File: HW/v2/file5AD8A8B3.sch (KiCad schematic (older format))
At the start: 45 parts, among them J14 Barrel_Jack, U17 LT1054 neg5v, U18 INA219, U19 LM7805, U20 LM1117-3.3, U21 Vref, U22 AD8628, U23 LM321

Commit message: friday layout
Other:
- note added: "Neg supply"
- note added: "vREF"
- moved on the sheet: C33, C34, C36, C37, C38, C40, C42, D5, D6, D7, D8, D9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

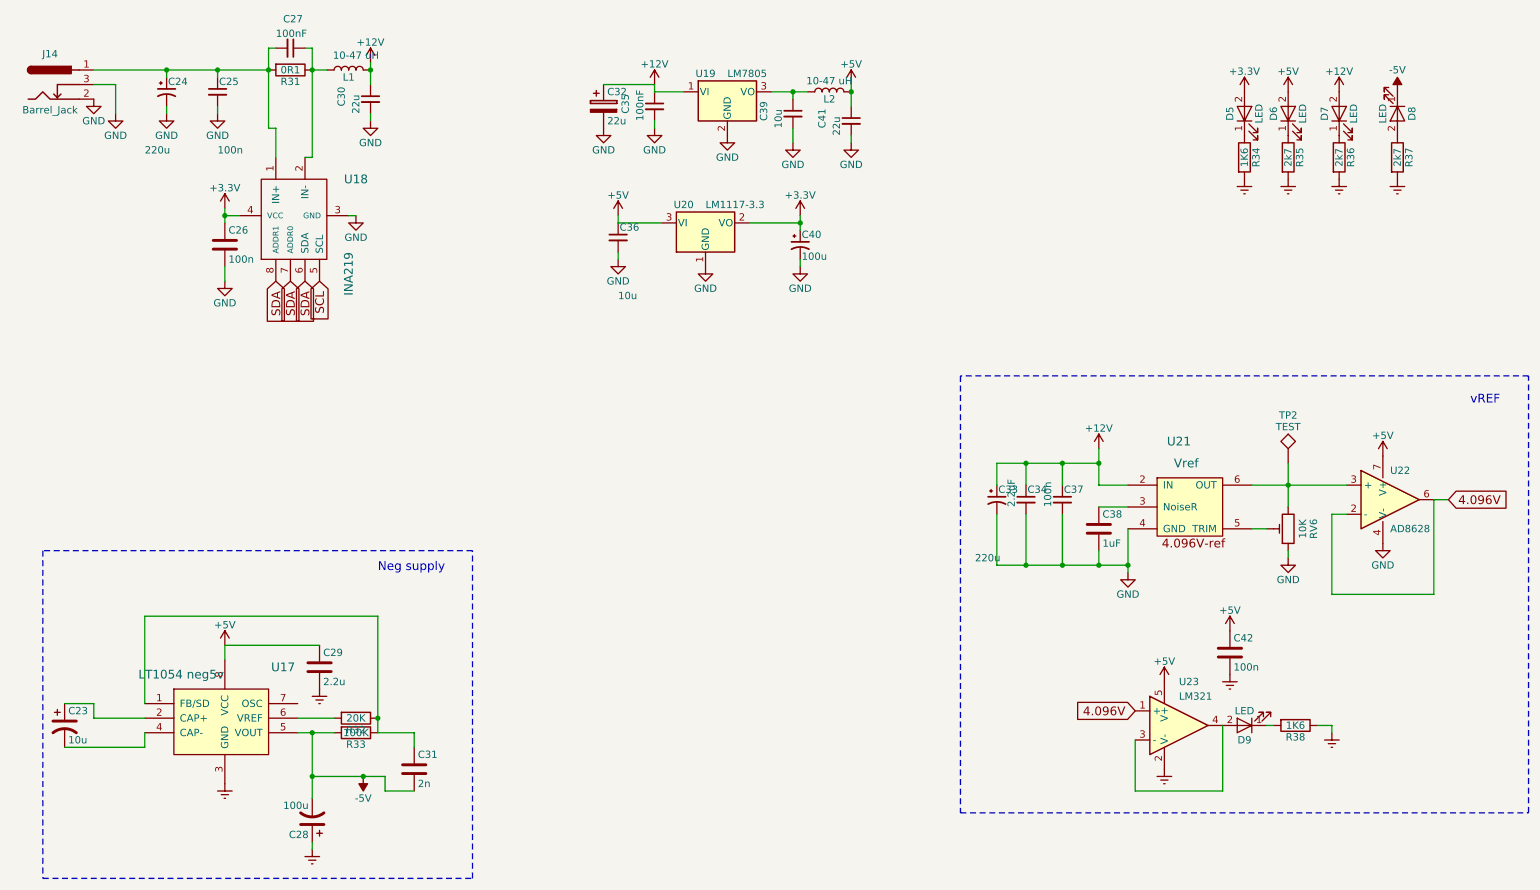
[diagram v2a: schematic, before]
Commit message: i2c pots for calibrating
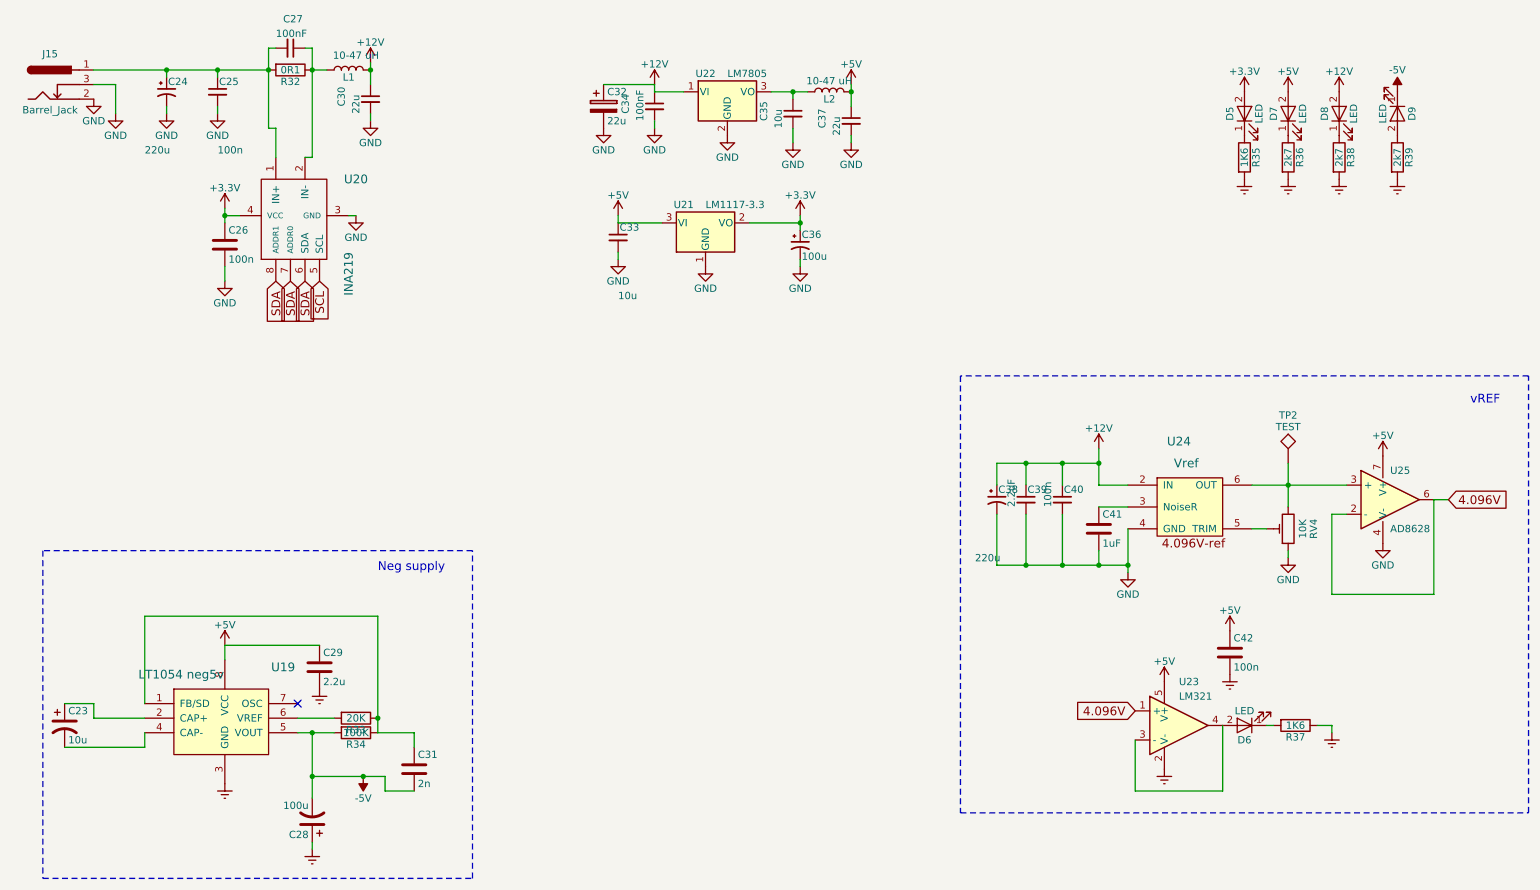
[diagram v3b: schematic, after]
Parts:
- renumbered C36 to C33, C35 to C34, C39 to C35, C40 to C36, C41 to C37, C33 to C38, C34 to C39, C37 to C40, C38 to C41, D9 to D6, D6 to D7, D7 to D8, D8 to D9, J14 to J15, R31 to R32, R32 to R33, R33 to R34, R34 to R35, R35 to R36, R38 to R37, R36 to R38, R37 to R39, RV6 to RV4, U17 to U19, U18 to U20, U20 to U21, U19 to U22, U21 to U24, U22 to U25
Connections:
- no-connect marks 0 -> 1

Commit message: v2 done
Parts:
- removed C42: 100n, Capacitors_SMD:C_0805_HandSoldering, symbol C
- removed D5, D6, D7, D8, D9: LED, LEDs:LED_0805_HandSoldering, symbol LED
- removed R35, R37: 1K6, Resistors_SMD:R_0805_HandSoldering, symbol R
- removed R36, R38, R39: 2k7, Resistors_SMD:R_0805_HandSoldering, symbol R
- removed U23: LM321, TO_SOT_Packages_SMD:SOT-23-5, symbol LM321
- renumbered C23 to C24, C24 to C25, C25 to C26, C26 to C27, C27 to C28, C28 to C29, C29 to C30, C30 to C31, C31 to C32, C32 to C33, C33 to C34, C34 to C35, C35 to C36, C36 to C37, C37 to C38, C38 to C39, C39 to C40, C40 to C41, C41 to C42

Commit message: more
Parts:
- C24, C29: symbol CP1 -> device:CP1
- C25, C37, C39: symbol CP1_Small -> device:CP1_Small
- C26, C28, C31, C34, C35, C36, C38, C40, C41: symbol C_Small -> device:C_Small
- C27, C30, C32, C42: symbol C -> device:C
- C33: symbol CP -> device:CP
- J15: symbol Barrel_Jack -> conn:Barrel_Jack
- L1, L2: symbol L -> device:L
- R32, R33, R34: symbol R -> device:R
- U19: symbol LT1054 -> Peters:LT1054
- U20: symbol INA219 -> Peters:INA219
- U21: symbol LM1117-3.3 -> regul:LM1117-3.3
- U22: symbol LM7805_TO220 -> regul:LM7805_TO220
- U24: symbol MAX6241 -> Peters:MAX6241
- U25: symbol AD8628 -> Peters:AD8628
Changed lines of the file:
@@
-EESchema Schematic File Version 2
-LIBS:power
-LIBS:device
-LIBS:switches
-LIBS:relays
-LIBS:motors
-LIBS:transistors
-LIBS:conn
-LIBS:linear
-LIBS:regul
-LIBS:74xx
-LIBS:cmos4000
-LIBS:adc-dac
-LIBS:memory
-LIBS:xilinx
-LIBS:microcontrollers
-LIBS:dsp
-LIBS:microchip
-LIBS:analog_switches
-LIBS:motorola
-LIBS:texas
-LIBS:intel
-LIBS:audio
-LIBS:interface
-LIBS:digital-audio
-LIBS:philips
-LIBS:display
-LIBS:cypress
-LIBS:siliconi
-LIBS:opto
-LIBS:atmel
-LIBS:contrib
-LIBS:valves
-LIBS:Peters
-LIBS:BLUEPILL
+EESchema Schematic File Version 4
 LIBS:v2-cache
-EELAYER 25 0
+EELAYER 26 0
 EELAYER END
 $Descr A4 11693 8268
@@
 $EndDescr
 $Comp
-L +3.3V #PWR0110
+L power:+3.3V #PWR0110
 U 1 1 5ADA7C90
 P 2100 2300
@@
 $EndComp
 $Comp
-L +12V #PWR0111
+L power:+12V #PWR0111
 U 1 1 5ADA7C91
 P 5050 1450
@@
 $EndComp
 $Comp
-L +5V #PWR0112
+L power:+5V #PWR0112
 U 1 1 5ADA7C92
 P 6400 1450
@@
 $EndComp
 $Comp
-L GND #PWR0113
+L power:GND #PWR0113
 U 1 1 5ADA7C93
 P 6000 1850
@@
 $EndComp
 $Comp
-L GND #PWR0114
+L power:GND #PWR0114
 U 1 1 5ADA7C94
 P 5050 1750
@@
 $EndComp
 $Comp
-L C_Small C35
+L device:C_Small C35
 U 1 1 5ADA7C95
 P 5050 1600
@@
 $EndComp
 $Comp
-L GND #PWR0115
+L power:GND #PWR0115
 U 1 1 5ADA7C96
 P 2050 1650
@@
 $EndComp
 $Comp
-L C_Small C26
+L device:C_Small C26
 U 1 1 5ADA7C97
 P 2050 1500
@@
 $EndComp
 $Comp
-L GND #PWR0116
+L power:GND #PWR0116
 U 1 1 5ADA7C98
 P 1700 1650
@@
 $EndComp
 $Comp
-L CP1_Small C25
+L device:CP1_Small C25
 U 1 1 5ADA7C99
 P 1700 1500
@@
 SDA
 $Comp
-L GND #PWR0117
+L power:GND #PWR0117
 U 1 1 5ADA7C9A
 P 3000 2350
@@
 $EndComp
 $Comp
-L R R32
+L device:R R32
 U 1 1 5ADA7C9B
 P 2550 1350
@@
 $EndComp
 $Comp
-L GND #PWR0118
+L power:GND #PWR0118
 U 1 1 5ADA7C9D
 P 1350 1650
@@
 $EndComp
 $Comp
-L +12V #PWR0119
+L power:+12V #PWR0119
 U 1 1 5ADA7C9E
 P 3100 1300
@@
 $EndComp
 $Comp
-L INA219 U20
+L Peters:INA219 U20
 U 1 1 5ADA7C9F
 P 2300 2350
@@
 $EndComp
 $Comp
-L C_Small C41
+L device:C_Small C41
 U 1 1 5ADA7CA0
 P 7850 4300
@@
 $EndComp
 $Comp
-L +12V #PWR0120
+L power:+12V #PWR0120
 U 1 1 5ADA7CA1
 P 8100 3950
@@
 $EndComp
 $Comp
-L GND #PWR0121
+L power:GND #PWR0121
 U 1 1 5ADA7CA2
 P 8300 4800
@@
 $EndComp
 $Comp
-L GND #PWR0122
+L power:GND #PWR0122
 U 1 1 5ADA7CA3
 P 4800 2650
@@
 $EndComp
 $Comp
-L C_Small C34
+L device:C_Small C34
 U 1 1 5ADA7CA4
 P 4800 2500
@@
 $EndComp
 $Comp
-L +5V #PWR0123
+L power:+5V #PWR0123
 U 1 1 5ADA7CA5
 P 4800 2350
@@
 $EndComp
 $Comp
-L +3.3V #PWR0124
+L power:+3.3V #PWR0124
 U 1 1 5ADA7CA6
 P 6050 2350
@@
 $EndComp
 $Comp
-L GND #PWR0125
+L power:GND #PWR0125
 U 1 1 5ADA7CA7
 P 6050 2700
@@
 	6050 2650 6050 2700
 $Comp
-L GND #PWR0126
+L power:GND #PWR0126
 U 1 1 5ADA7CA9
 P 5400 2700
@@
 $EndComp
 $Comp
-L -5V #PWR130
+L power:-5V #PWR130
 U 1 1 5ADA7CAA
 P 3050 6200
@@
 $EndComp
 $Comp
-L LT1054 U19
+L Peters:LT1054 U19
 U 1 1 5ADA7CAB
 P 2100 6000
@@
 $EndComp
 $Comp
-L CP1 C24
+L device:CP1 C24
 U 1 1 5ADA7CAC
 P 1000 5850
@@
 $EndComp
 $Comp
-L R R33
+L device:R R33
 U 1 1 5ADA7CAD
 P 3000 5800
@@
 $EndComp
 $Comp
-L R R34
+L device:R R34
 U 1 1 5ADA7CAE
 P 3000 5900
@@
 $EndComp
 $Comp
-L +5V #PWR0127
+L power:+5V #PWR0127
 U 1 1 5ADA7CAF
 P 2100 5300
@@
 $EndComp
 $Comp
-L Earth #PWR0128
+L power:Earth #PWR0128
 U 1 1 5ADA7CB0
 P 2100 6250
@@
 Connection ~ 2700 5900
 $Comp
-L CP1 C29
+L device:CP1 C29
 U 1 1 5ADA7CB1
 P 2700 6500
@@
 $EndComp
 $Comp
-L Earth #PWR0129
+L power:Earth #PWR0129
 U 1 1 5ADA7CB2
 P 2700 6700
@@
 Connection ~ 2700 6200
 $Comp
-L C C32
+L device:C C32
 U 1 1 5ADA7CB3
 P 3400 6150
@@
 Connection ~ 3050 6200
 $Comp
-L C C30
+L device:C C30
 U 1 1 5ADA7CB4
 P 2750 5450
@@
 	2750 5300 2100 5300
 $Comp
-L Earth #PWR0130
+L power:Earth #PWR0130
 U 1 1 5ADA7CB5
 P 2750 5600
@@
 	6000 1750 6000 1850
 $Comp
-L MAX6241 U24
+L Peters:MAX6241 U24
 U 1 1 5ADA7CB8
 P 8750 3800
@@
 Connection ~ 8100 4050
 $Comp
-L C C42
+L device:C C42
 U 1 1 5ADA7CB9
 P 8100 4500
@@
 4.096V
 $Comp
-L C C27
+L device:C C27
 U 1 1 5ADA7CBD
 P 2100 2550
@@
 $EndComp
 $Comp
-L GND #PWR0131
+L power:GND #PWR0131
 U 1 1 5ADA7CBE
 P 2100 2800
@@
 Connection ~ 2100 2350
 $Comp
-L Barrel_Jack J15
+L conn:Barrel_Jack J15
 U 1 1 5ADA831E
 P 900 1450
@@
 $EndComp
 $Comp
-L GND #PWR0144
+L power:GND #PWR0144
 U 1 1 5ADA843B
 P 1200 1550
@@
 	9250 4500 9150 4500
 $Comp
-L GND #PWR0145
+L power:GND #PWR0145
 U 1 1 5ADA8F5A
 P 9400 4700
@@
 	9400 4650 9400 4700
 $Comp
-L C_Small C40
+L device:C_Small C40
 U 1 1 5ADA9080
 P 7600 4300
@@
 Connection ~ 7600 4750
 $Comp
-L CP1_Small C39
+L device:CP1_Small C39
 U 1 1 5ADA99FF
 P 7400 4300
@@
 $EndComp
 $Comp
-L AD8628 U25
+L Peters:AD8628 U25
 U 1 1 5ADAAA51
 P 10100 4300
@@
 $EndComp
 $Comp
-L GND #PWR0146
+L power:GND #PWR0146
 U 1 1 5ADAAC56
 P 10050 4600
@@
 Connection ~ 9400 4200
 $Comp
-L +5V #PWR0147
+L power:+5V #PWR0147
 U 1 1 5ADAAFA1
 P 10050 4000
@@
 $EndComp
 $Comp
-L LM1117-3.3 U21
+L regul:LM1117-3.3 U21
 U 1 1 5ADAB666
 P 5400 2400
@@
 $EndComp
 $Comp
-L CP1_Small C37
+L device:CP1_Small C37
 U 1 1 5ADABA11
 P 6050 2550
@@
 Connection ~ 6050 2400
 $Comp
-L LM7805_TO220 U22
+L regul:LM7805_TO220 U22
 U 1 1 5ADABE82
 P 5550 1500
@@
 $EndComp
 $Comp
-L C_Small C28
+L device:C_Small C28
 U 1 1 5ADABF9E
 P 2550 1200
@@
 Connection ~ 2700 1350
 $Comp
-L C_Small C36
+L device:C_Small C36
 U 1 1 5ADAC218
 P 6000 1650
@@
 $EndComp
 $Comp
-L CP C33
+L device:CP C33
 U 1 1 5ADAC477
 P 4700 1600
@@
 $EndComp
 $Comp
-L GND #PWR0148
+L power:GND #PWR0148
 U 1 1 5ADAC5F2
 P 4700 1750
@@
 	5050 1450 4700 1450
 $Comp
-L GND #PWR0149
+L power:GND #PWR0149
 U 1 1 5ADAC870
 P 5550 1800
@@
 $EndComp
 $Comp
-L L L2
+L device:L L2
 U 1 1 5ADAC8CD
 P 6250 1500
@@
 $EndComp
 $Comp
-L C_Small C38
+L device:C_Small C38
 U 1 1 5ADAC999
 P 6400 1700
@@
 $EndComp
 $Comp
-L GND #PWR0150
+L power:GND #PWR0150
 U 1 1 5ADACA3B
 P 6400 1850
@@
 $EndComp
 $Comp
-L L L1
+L device:L L1
 U 1 1 5ADB4139
 P 2950 1350
@@
 $EndComp
 $Comp
-L C_Small C31
+L device:C_Small C31
 U 1 1 5ADB413F
 P 3100 1550
@@
 $EndComp
 $Comp
-L GND #PWR0151
+L power:GND #PWR0151
 U 1 1 5ADB4145
 P 3100 1700
